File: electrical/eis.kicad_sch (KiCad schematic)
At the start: 33 parts

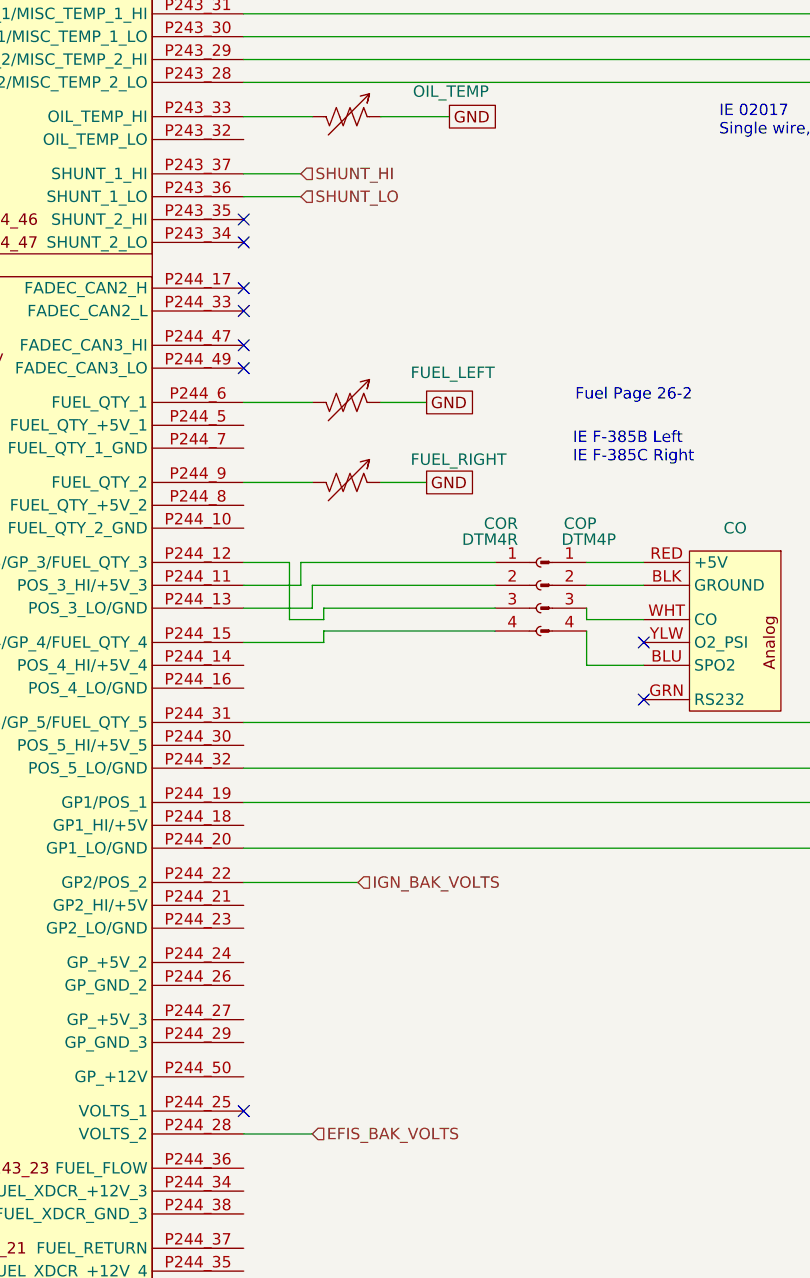
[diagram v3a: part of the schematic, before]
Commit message: Changed power outputs on VP-X to match sides the LRU's are on. Also, removed Shunt from wiring and just use VP-X for Amperage.
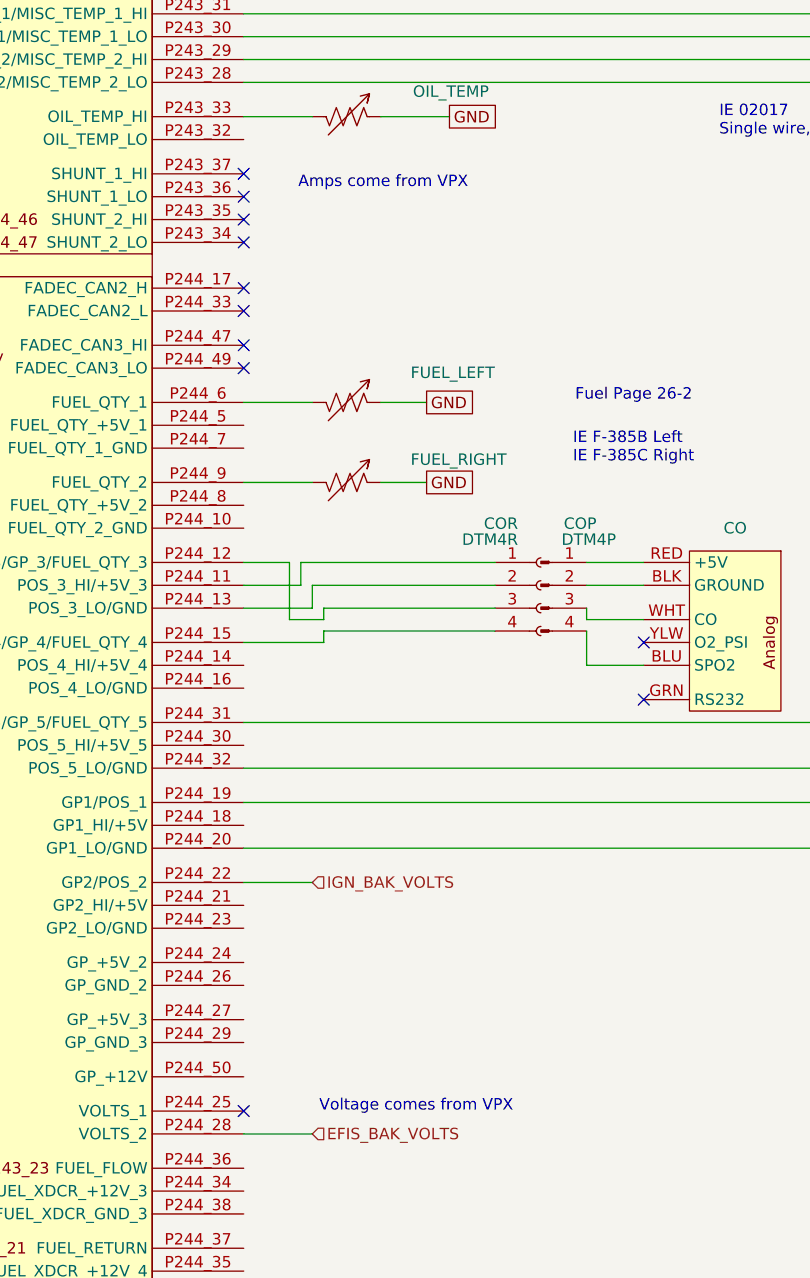
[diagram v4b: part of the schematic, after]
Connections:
- net SHUNT_HI: no longer names the net of GEA24.P243_37 (SHUNT_1_HI)
- net SHUNT_LO: no longer names the net of GEA24.P243_36 (SHUNT_1_LO)
- no-connect marks 19 -> 21
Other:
- note added: "Amps come from VPX"
- note added: "Voltage comes from VPX"
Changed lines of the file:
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@@
 	(title_block
 		(title "EIS")
-		(date "2025-09-25")
-		(rev "1.0.6")
+		(date "2025-09-29")
+		(rev "1.0.7")
 		(company "N78HR")
 	)
@@
 		)
 	)
+	(text "Amps come from VPX"
+		(exclude_from_sim no)
+		(at 82.804 206.756 0)
+		(effects
+			(font
+				(size 1.27 1.27)
+			)
+		)
+	)
 	(text "Reusing US-8A Connector / Wiring"
 		(exclude_from_sim no)
@@
 		(exclude_from_sim no)
 		(at 103.886 236.22 0)
+		(effects
+			(font
+				(size 1.27 1.27)
+			)
+			(justify left)
+		)
+	)
+	(text "Voltage comes from VPX"
+		(exclude_from_sim no)
+		(at 75.692 309.372 0)
 		(effects
 			(font
@@
 	)
 	(no_connect
+		(at 67.31 208.28)
+	)
+	(no_connect
 		(at 95.25 134.62)
 	)
@@
 		(at 67.31 137.16)
 	)
+	(no_connect
+		(at 67.31 205.74)
+	)
 	(wire
 		(pts
@@
 	(wire
 		(pts
-			(xy 67.31 208.28) (xy 73.66 208.28)
-		)
-		(stroke
-			(width 0)
-			(type default)
-		)
-	)
-	(wire
-		(pts
 			(xy 173.99 142.24) (xy 189.23 142.24)
 		)
@@
 	(wire
 		(pts
-			(xy 67.31 284.48) (xy 80.01 284.48)
+			(xy 67.31 284.48) (xy 74.93 284.48)
 		)
 		(stroke
@@
 		(pts
 			(xy 210.82 134.62) (xy 210.82 132.08)
-		)
-		(stroke
-			(width 0)
-			(type default)
-		)
-	)
-	(wire
-		(pts
-			(xy 67.31 205.74) (xy 73.66 205.74)
 		)
 		(stroke
@@
 		)
 	)
-	(hierarchical_label "SHUNT_LO"
-		(shape input)
-		(at 73.66 208.28 0)
-		(effects
-			(font
-				(size 1.27 1.27)
-			)
-			(justify left)
-		)
-	)
 	(hierarchical_label "SERIAL_GND"
 		(shape passive)
@@
 	(hierarchical_label "IGN_BAK_VOLTS"
 		(shape input)
-		(at 80.01 284.48 0)
+		(at 74.93 284.48 0)
 		(effects
 			(font
@@
 		(effects
 			(font
-				(size 1.27 1.27)
-			)
-			(justify left)
-		)
-	)
-	(hierarchical_label "SHUNT_HI"
-		(shape input)
-		(at 73.66 205.74 0)
-		(effects
-			(font

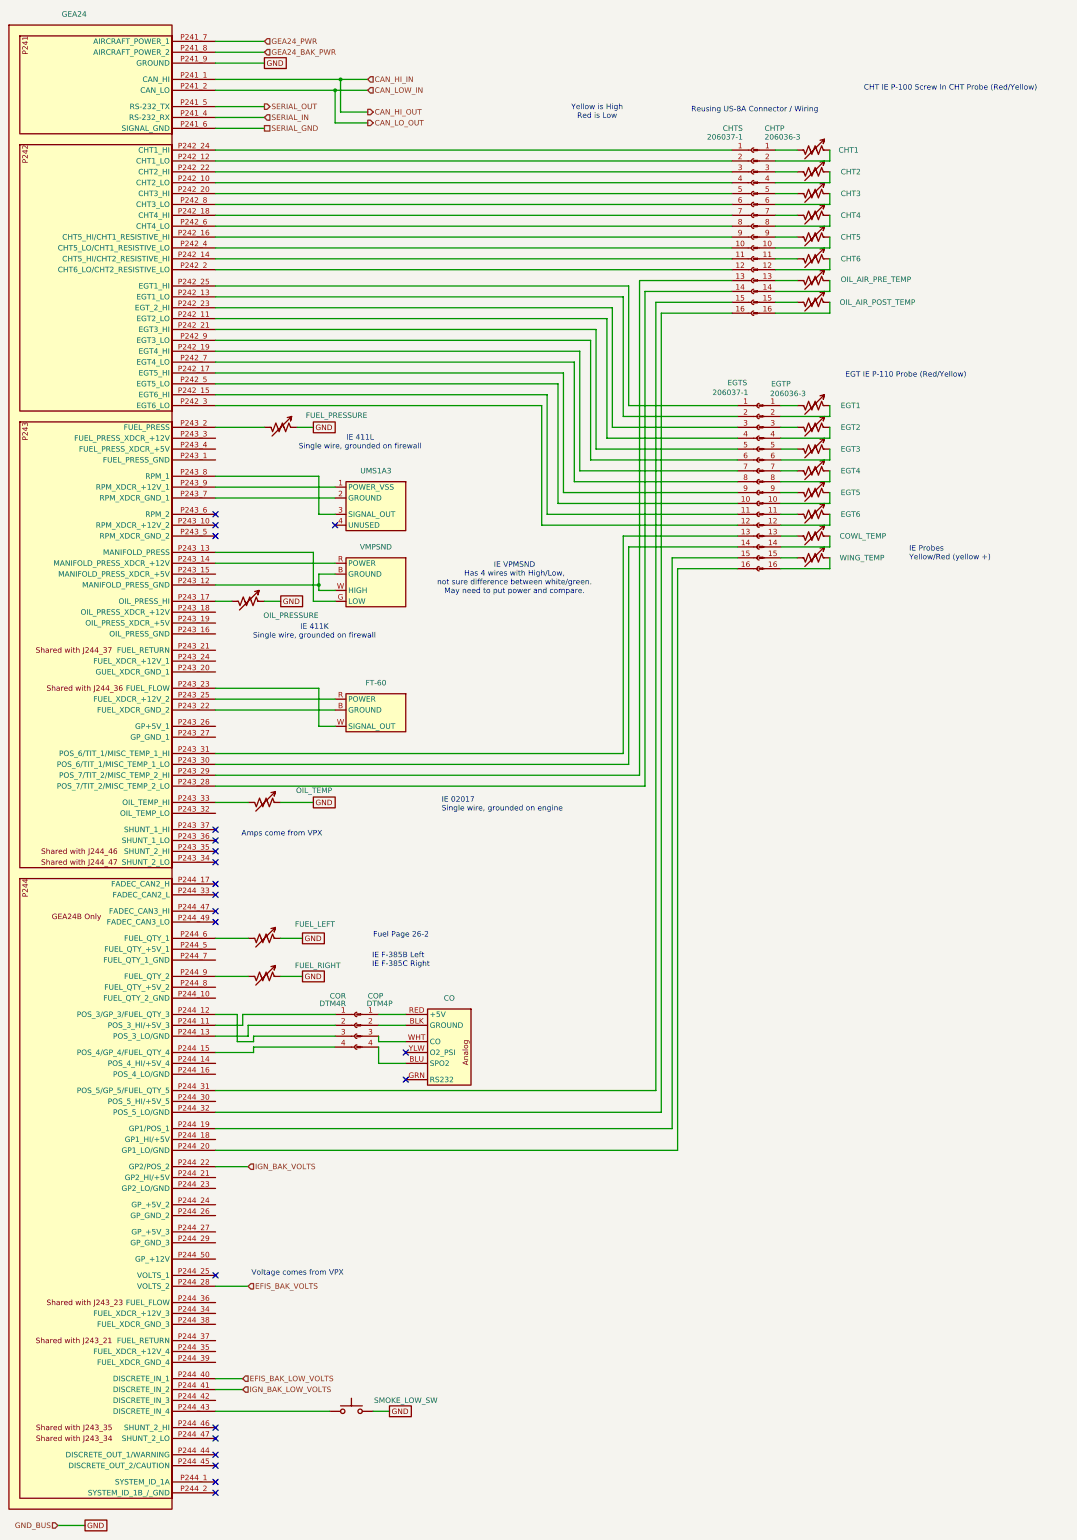
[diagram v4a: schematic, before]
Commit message: Added connectors and non-CAN/RS232/Ethernet shields.
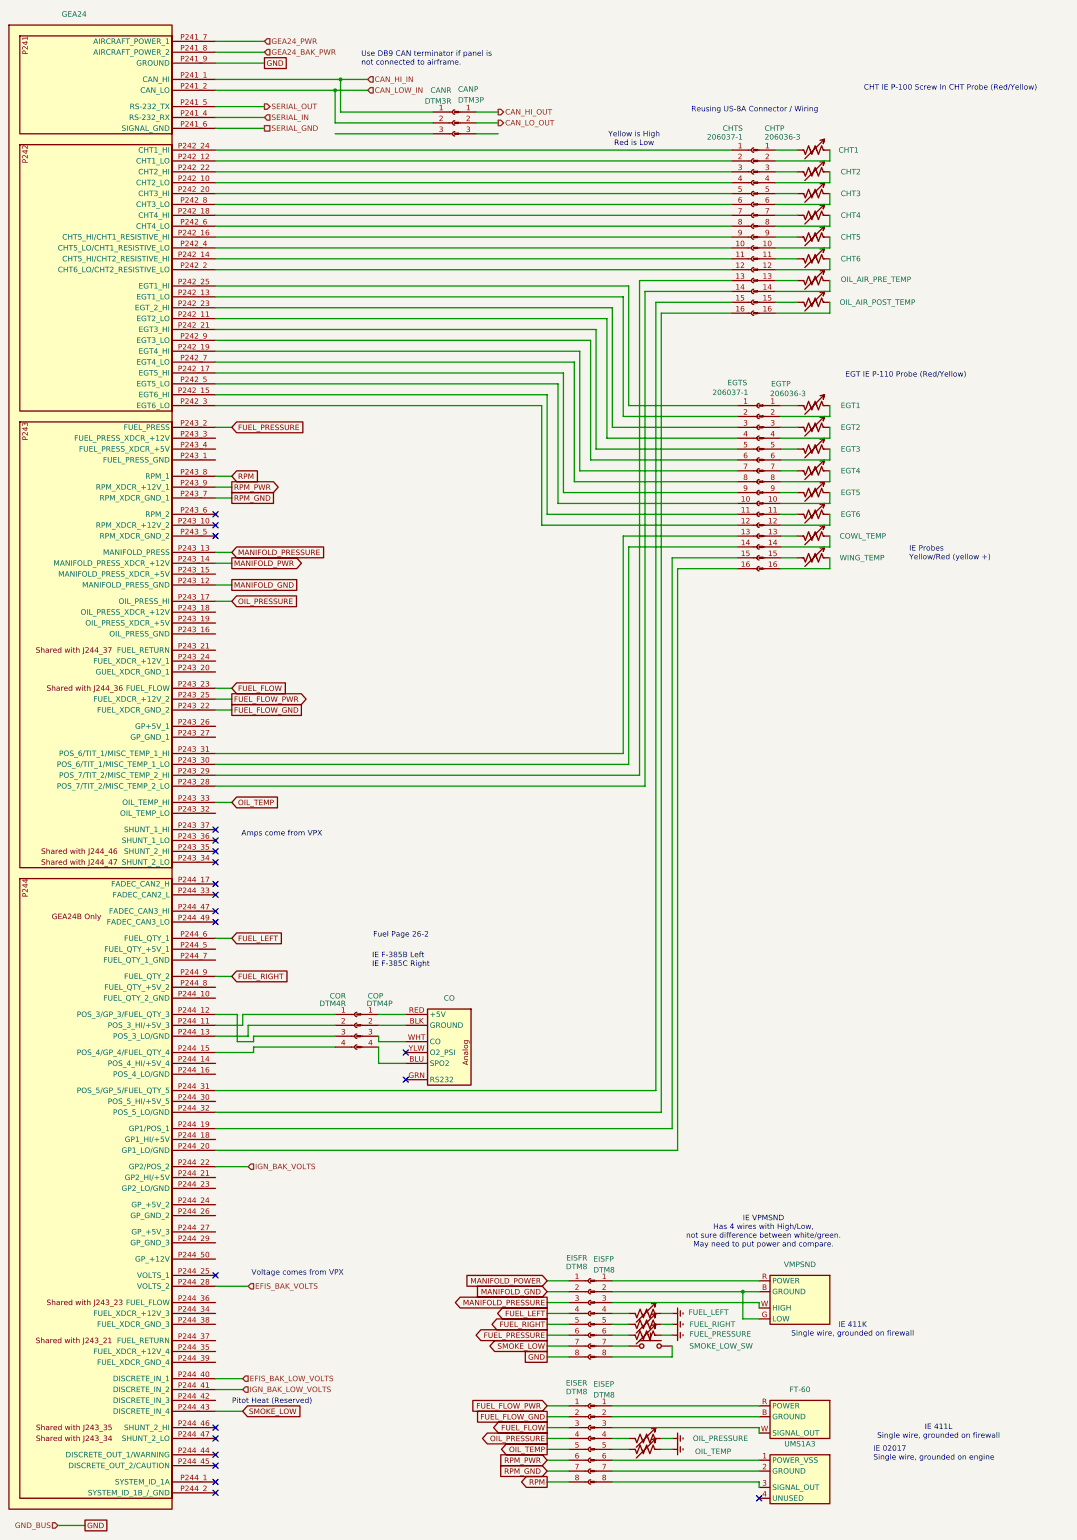
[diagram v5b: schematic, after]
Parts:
- added CANP: DTM3P, symbol Connector:Conn_01x03_Pin
- added CANR: DTM3R, symbol Connector:Conn_01x03_Socket
- added EISEP, EISFP: DTM8, symbol Connector:Conn_01x08_Pin
- added EISER, EISFR: DTM8, symbol Connector:Conn_01x08_Socket
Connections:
- net CAN_HI_IN: now also CANR.1 (Pin_1)
- net CAN_LOW_IN: now also CANR.2 (Pin_2)
- net GND: now also EISFR.8 (Pin_8); no longer FUEL_LEFT.1, FUEL_PRESSURE.1, FUEL_RIGHT.1, OIL_PRESSURE.1, OIL_TEMP.1, SMOKE_LOW_SW.2
- net at FUEL_PRESSURE.2: now also EISFP.6 (Pin_6); no longer GEA24.P243_2 (FUEL_PRESS)
- net at FT-60.B (GROUND): now also EISEP.2 (Pin_2); no longer GEA24.P243_22 (FUEL_XDCR_GND_2)
- net at FT-60.R (POWER): now also EISEP.1 (Pin_1); no longer GEA24.P243_25 (FUEL_XDCR_+12V_2)
- net at FT-60.W (SIGNAL_OUT): now also EISEP.3 (Pin_3); no longer GEA24.P243_23 (FUEL_FLOW)
- net at VMPSND.G (LOW): now also VMPSND.B (GROUND), EISFP.2 (Pin_2); no longer GEA24.P243_13 (MANIFOLD_PRESS)
- net at VMPSND.R (POWER): now also EISFP.1 (Pin_1); no longer GEA24.P243_14 (MANIFOLD_PRESS_XDCR_+12V)
- net at OIL_PRESSURE.2: now also EISEP.4 (Pin_4); no longer GEA24.P243_17 (OIL_PRESS_HI)
- net at OIL_TEMP.2: now also EISEP.5 (Pin_5); no longer GEA24.P243_33 (OIL_TEMP_HI)
- net at UMS1A3.2 (GROUND): now also EISEP.7 (Pin_7); no longer GEA24.P243_7 (RPM_XDCR_GND_1)
- net at UMS1A3.3 (SIGNAL_OUT): now also EISEP.8 (Pin_8); no longer GEA24.P243_8 (RPM_1)
- net at UMS1A3.1 (POWER_VSS): now also EISEP.6 (Pin_6); no longer GEA24.P243_9 (RPM_XDCR_+12V_1)
- net at SMOKE_LOW_SW.1: now also EISFP.7 (Pin_7); no longer GEA24.P244_43 (DISCRETE_IN_4)
- net at FUEL_LEFT.2: now also EISFP.4 (Pin_4); no longer GEA24.P244_6 (FUEL_QTY_1)
- net at FUEL_RIGHT.2: now also EISFP.5 (Pin_5); no longer GEA24.P244_9 (FUEL_QTY_2)
- new net: EISFP.3 (Pin_3), VMPSND.W (HIGH)
- new net: EISFP.8 (Pin_8), SMOKE_LOW_SW.2
- new net CAN_HI_OUT: CANP.1 (Pin_1)
- new net CAN_LO_OUT: CANP.2 (Pin_2)
- new net Earth: FUEL_LEFT.1, FUEL_PRESSURE.1, FUEL_RIGHT.1, OIL_PRESSURE.1, OIL_TEMP.1
- new net FUEL_FLOW: EISER.3 (Pin_3), GEA24.P243_23 (FUEL_FLOW)
- new net FUEL_FLOW_GND: EISER.2 (Pin_2), GEA24.P243_22 (FUEL_XDCR_GND_2)
- new net FUEL_FLOW_PWR: EISER.1 (Pin_1), GEA24.P243_25 (FUEL_XDCR_+12V_2)
- new net FUEL_LEFT: EISFR.4 (Pin_4), GEA24.P244_6 (FUEL_QTY_1)
- new net FUEL_PRESSURE: EISFR.6 (Pin_6), GEA24.P243_2 (FUEL_PRESS)
- new net FUEL_RIGHT: EISFR.5 (Pin_5), GEA24.P244_9 (FUEL_QTY_2)
- new net MANIFOLD_GND: EISFR.2 (Pin_2), GEA24.P243_12 (MANIFOLD_PRESS_GND)
- new net MANIFOLD_POWER: EISFR.1 (Pin_1)
- new net MANIFOLD_PRESSURE: EISFR.3 (Pin_3), GEA24.P243_13 (MANIFOLD_PRESS)
- new net MANIFOLD_PWR: GEA24.P243_14 (MANIFOLD_PRESS_XDCR_+12V)
- new net OIL_PRESSURE: EISER.4 (Pin_4), GEA24.P243_17 (OIL_PRESS_HI)
- new net OIL_TEMP: EISER.5 (Pin_5), GEA24.P243_33 (OIL_TEMP_HI)
- new net RPM: EISER.8 (Pin_8), GEA24.P243_8 (RPM_1)
- new net RPM_GND: EISER.7 (Pin_7), GEA24.P243_7 (RPM_XDCR_GND_1)
- new net RPM_PWR: EISER.6 (Pin_6), GEA24.P243_9 (RPM_XDCR_+12V_1)
- new net SMOKE_LOW: EISFR.7 (Pin_7), GEA24.P244_43 (DISCRETE_IN_4)
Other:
- note added: "Pitot Heat (Reserved)"
- note added: "Use DB9 CAN terminator if panel is not connected to airframe."
- moved on the sheet: FT-60, FUEL_LEFT, FUEL_PRESSURE, FUEL_RIGHT, OIL_PRESSURE, OIL_TEMP, SMOKE_LOW_SW, UMS1A3, VMPSND

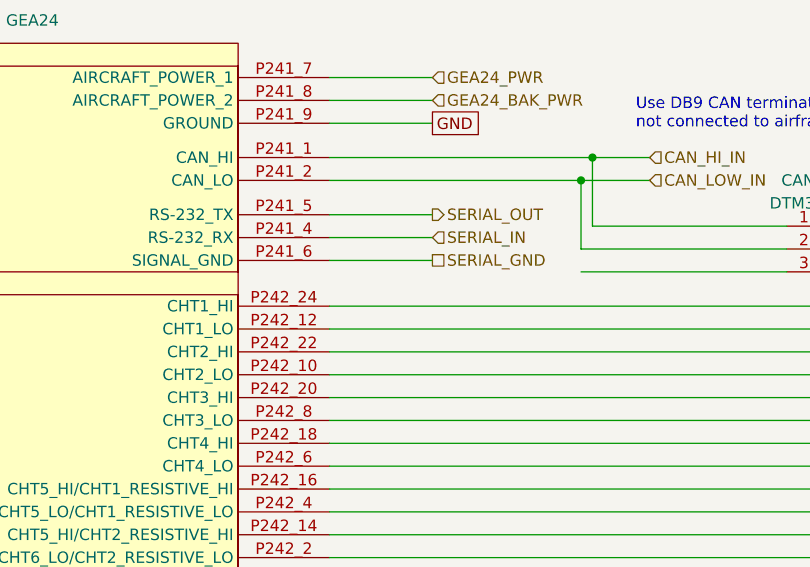
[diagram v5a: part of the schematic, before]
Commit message: Added RS232 and Canbus wiring notation
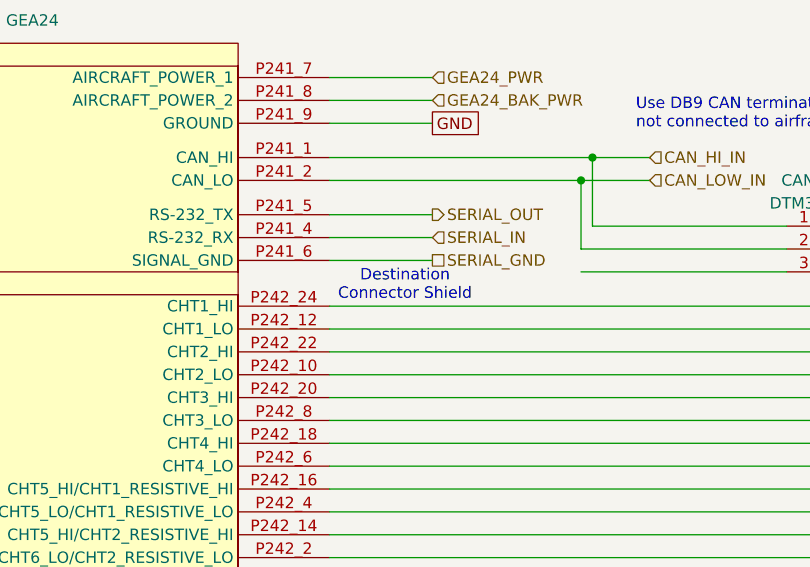
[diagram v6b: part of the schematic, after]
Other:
- note added: "Destination Connector Shield"
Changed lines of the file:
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@@
 	(title_block
 		(title "EIS")
-		(date "2025-10-01")
-		(rev "1.1")
+		(date "2025-10-02")
+		(rev "1.1.4")
 		(company "N78HR")
 	)
@@
 		(effects
 			(font
+				(size 1.27 1.27)
+			)
+		)
+	)
+	(text "Destination\nConnector Shield"
+		(exclude_from_sim no)
+		(at 75.692 44.704 0)
+		(effects
+			(font
